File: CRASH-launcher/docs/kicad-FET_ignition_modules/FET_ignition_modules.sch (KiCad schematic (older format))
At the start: 22 parts, among them P1 CONN_1, P1 CONN_6, P2 CONN_1, P2 CONN_2, P3 CONN_1, Q1 FET_N, Q2 FET_N, U1 TSC888, U2 TSC888

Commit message: second shot at module PCB
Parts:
- removed P1, P2: CONN_1, symbol CONN_1
- added P4: CONN_1, symbol CONN_1
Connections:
- net GNDPWR: now also P4.1
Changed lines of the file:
@@
-EESchema Schematic File Version 2  date Fri 15 Jun 2012 12:45:23 AM MDT
+EESchema Schematic File Version 2  date Fri 15 Jun 2012 01:25:22 AM MDT
 LIBS:bryan_custom
 LIBS:power
@@
 Comment4 ""
 $EndDescr
-Connection ~ 9450 6550
-Connection ~ 9450 6400
 $Comp
-L CONN_1 P2
-U 1 1 4FDAD9F2
-P 9600 6550
-F 0 "P2" H 9680 6550 40  0000 L CNN
-F 1 "CONN_1" H 9600 6605 30  0001 C CNN
-	1    9600 6550
-	1    0    0    -1
-$EndComp
-$Comp
-L CONN_1 P1
-U 1 1 4FDAD9EC
+L CONN_1 P4
+U 1 1 4FDADA40
 P 9600 6400
-F 0 "P1" H 9680 6400 40  0000 L CNN
+F 0 "P4" H 9680 6400 40  0000 L CNN
 F 1 "CONN_1" H 9600 6455 30  0001 C CNN
 	1    9600 6400
 	1    0    0    -1
 $EndComp
-Connection ~ 7100 3500
 $Comp
 L CONN_1 P3
-U 1 1 4FDAD9BF
+U 1 1 4FDADA3B
 P 7250 3500
 F 0 "P3" H 7330 3500 40  0000 L CNN
@@
 	1    0    0    -1
 $EndComp
+Connection ~ 9450 6400
+Connection ~ 7100 3500
 Connection ~ 5500 3900
 Wire Wire Line

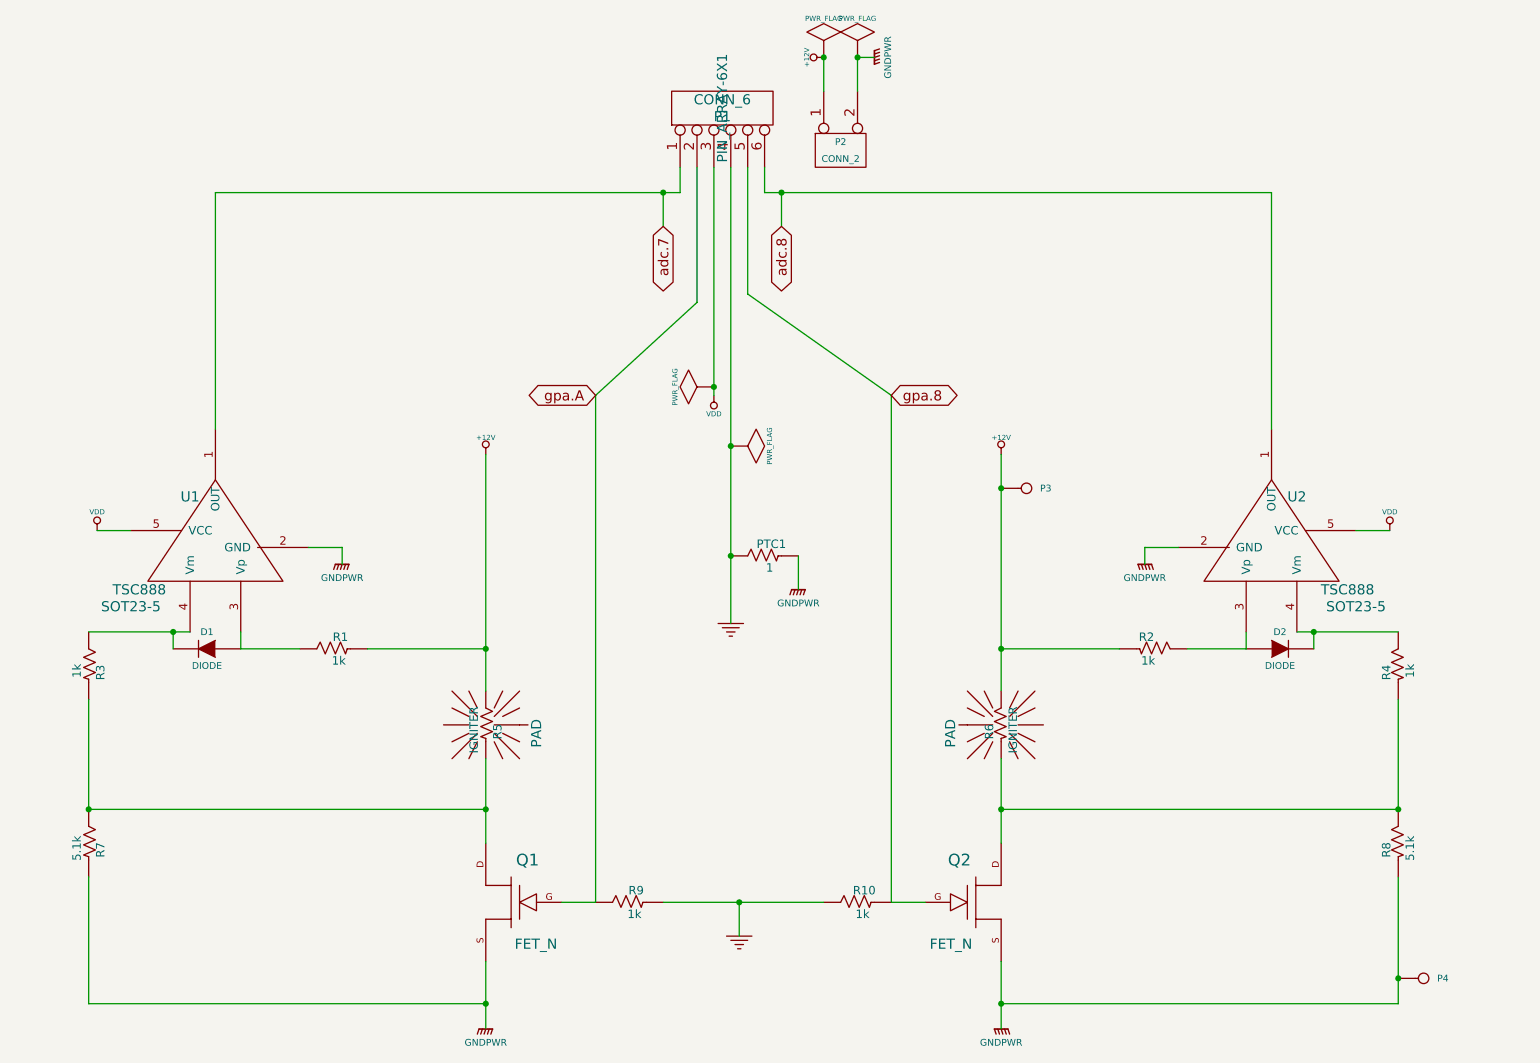
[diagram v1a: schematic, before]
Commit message: rounded corners on PCB zones, removed VDD rectangle, other suggestions from sgrace
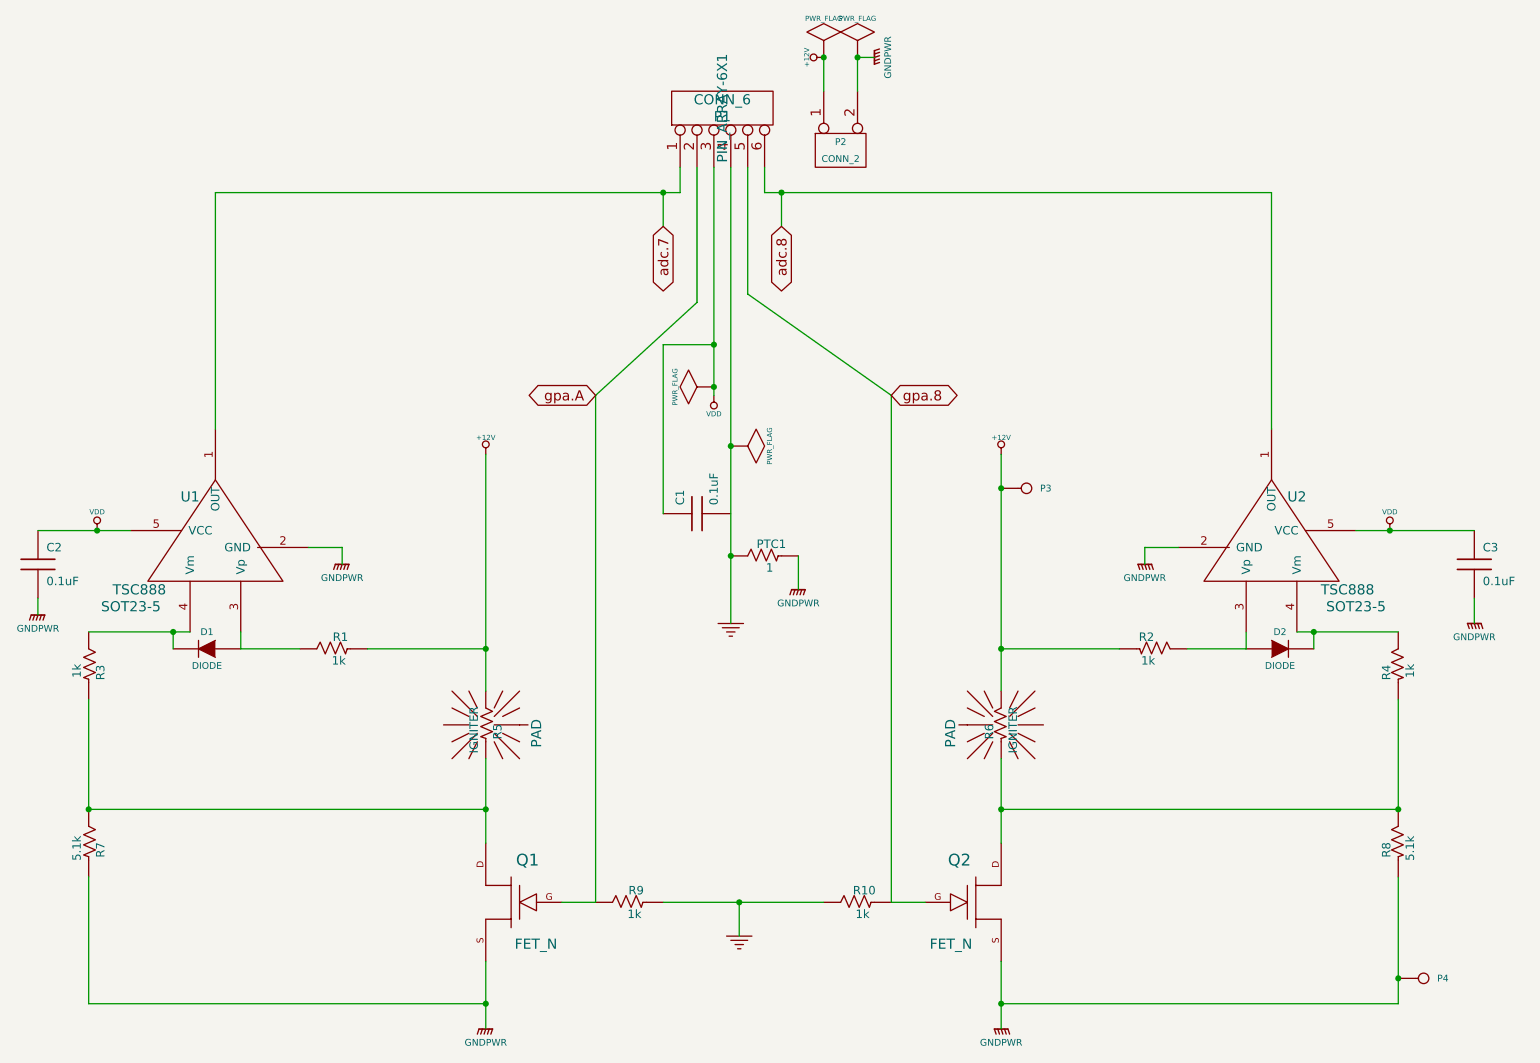
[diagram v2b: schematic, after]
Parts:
- added C1, C2, C3: 0.1uF, symbol C
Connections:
- net GNDPWR: now also C2.2, C3.2
- net VDD: now also C1.1, C2.1, C3.1

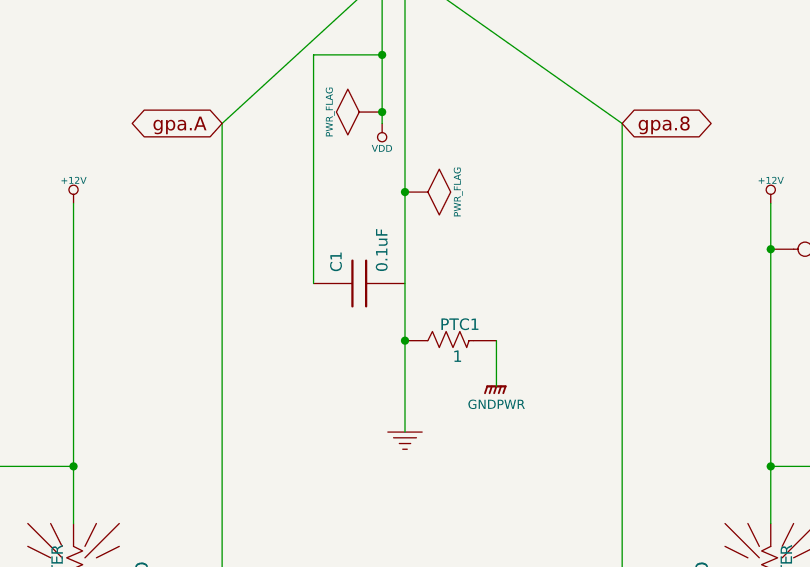
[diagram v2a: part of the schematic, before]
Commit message: rounded corners, plopped in a few missing caps on gpios and adc
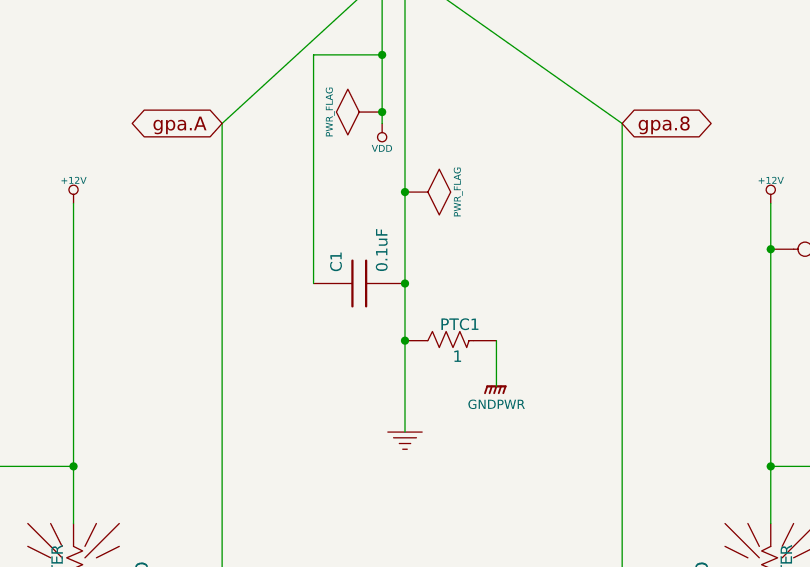
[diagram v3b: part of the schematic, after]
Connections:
- net GND: now also C1.2
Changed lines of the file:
@@
-EESchema Schematic File Version 2  date Fri 15 Jun 2012 06:22:16 PM MDT
+EESchema Schematic File Version 2  date Tue 03 Jul 2012 10:38:54 AM MDT
 LIBS:bryan_custom
 LIBS:power
@@
 Sheet 1 1
 Title ""
-Date "16 jun 2012"
+Date "17 jun 2012"
 Rev ""
 Comp ""
@@
 Comment4 ""
 $EndDescr
+Connection ~ 5500 3650
 Connection ~ 5400 2650
 Wire Wire Line
@@
 $EndComp
 $Comp
-L GNDPWR #PWR13
+L GNDPWR #PWR01
 U 1 1 4FDBCF69
 P 9900 4300
-F 0 "#PWR13" H 9900 4350 40  0001 C CNN
+F 0 "#PWR01" H 9900 4350 40  0001 C CNN
 F 1 "GNDPWR" H 9900 4220 40  0000 C CNN
 	1    9900 4300
@@
 $EndComp
 $Comp
-L GNDPWR #PWR11
+L GNDPWR #PWR02
 U 1 1 4FDBCF4D
 P 1400 4250
-F 0 "#PWR11" H 1400 4300 40  0001 C CNN
+F 0 "#PWR02" H 1400 4300 40  0001 C CNN
 F 1 "GNDPWR" H 1400 4170 40  0000 C CNN
 	1    1400 4250
@@
 $EndComp
 $Comp
-L GNDPWR #PWR10
+L GNDPWR #PWR03
 U 1 1 4FD97A60
 P 5900 4100
-F 0 "#PWR10" H 5900 4150 40  0001 C CNN
+F 0 "#PWR03" H 5900 4150 40  0001 C CNN
 F 1 "GNDPWR" H 5900 4020 40  0000 C CNN
 	1    5900 4100
@@
 $EndComp
 $Comp
-L PWR_FLAG #FLG3
+L PWR_FLAG #FLG04
 U 1 1 4FD97533
 P 5400 2900
-F 0 "#FLG3" H 5400 3170 30  0001 C CNN
+F 0 "#FLG04" H 5400 3170 30  0001 C CNN
 F 1 "PWR_FLAG" H 5400 3130 30  0000 C CNN
 	1    5400 2900
@@
 $EndComp
 $Comp
-L GND #PWR14
+L GND #PWR05
 U 1 1 4FD9750F
 P 5550 6150
-F 0 "#PWR14" H 5550 6150 30  0001 C CNN
+F 0 "#PWR05" H 5550 6150 30  0001 C CNN
 F 1 "GND" H 5550 6080 30  0001 C CNN
 	1    5550 6150
@@
 $EndComp
 $Comp
-L PWR_FLAG #FLG4
+L PWR_FLAG #FLG06
 U 1 1 4FD974CA
 P 5500 3250
-F 0 "#FLG4" H 5500 3520 30  0001 C CNN
+F 0 "#FLG06" H 5500 3520 30  0001 C CNN
 F 1 "PWR_FLAG" H 5500 3480 30  0000 C CNN
 	1    5500 3250
@@
 $EndComp
 $Comp
-L PWR_FLAG #FLG1
+L PWR_FLAG #FLG07
 U 1 1 4FD974B2
 P 6050 950
-F 0 "#FLG1" H 6050 1220 30  0001 C CNN
+F 0 "#FLG07" H 6050 1220 30  0001 C CNN
 F 1 "PWR_FLAG" H 6050 1180 30  0000 C CNN
 	1    6050 950
@@
 $EndComp
 $Comp
-L PWR_FLAG #FLG2
+L PWR_FLAG #FLG08
 U 1 1 4FD974AA
 P 6250 950
-F 0 "#FLG2" H 6250 1220 30  0001 C CNN
+F 0 "#FLG08" H 6250 1220 30  0001 C CNN
 F 1 "PWR_FLAG" H 6250 1180 30  0000 C CNN
 	1    6250 950
@@
 $EndComp
 $Comp
-L +12V #PWR5
+L +12V #PWR09
 U 1 1 4FD97473
 P 7100 3300
-F 0 "#PWR5" H 7100 3250 20  0001 C CNN
+F 0 "#PWR09" H 7100 3250 20  0001 C CNN
 F 1 "+12V" H 7100 3400 30  0000 C CNN
 	1    7100 3300
@@
 $EndComp
 $Comp
-L VDD #PWR7
+L VDD #PWR010
 U 1 1 4FD973FA
 P 9400 3750
-F 0 "#PWR7" H 9400 3850 30  0001 C CNN
+F 0 "#PWR010" H 9400 3850 30  0001 C CNN
 F 1 "VDD" H 9400 3860 30  0000 C CNN
 	1    9400 3750
@@
 $EndComp
 $Comp
-L GNDPWR #PWR9
+L GNDPWR #PWR011
 U 1 1 4FD973F6
 P 7950 3950
-F 0 "#PWR9" H 7950 4000 40  0001 C CNN
+F 0 "#PWR011" H 7950 4000 40  0001 C CNN
 F 1 "GNDPWR" H 7950 3870 40  0000 C CNN
 	1    7950 3950
@@
 $EndComp
 $Comp
-L GNDPWR #PWR16
+L GNDPWR #PWR012
 U 1 1 4FD973F5
 P 7100 6700
-F 0 "#PWR16" H 7100 6750 40  0001 C CNN
+F 0 "#PWR012" H 7100 6750 40  0001 C CNN
 F 1 "GNDPWR" H 7100 6620 40  0000 C CNN
 	1    7100 6700
@@
 $EndComp
 $Comp
-L VDD #PWR3
+L VDD #PWR013
 U 1 1 4FD9738F
 P 5400 2950
-F 0 "#PWR3" H 5400 3050 30  0001 C CNN
+F 0 "#PWR013" H 5400 3050 30  0001 C CNN
 F 1 "VDD" H 5400 3060 30  0000 C CNN
 	1    5400 2950
@@
 $EndComp
 $Comp
-L GNDPWR #PWR15
+L GNDPWR #PWR014
 U 1 1 4FD97309
 P 4050 6700
-F 0 "#PWR15" H 4050 6750 40  0001 C CNN
+F 0 "#PWR014" H 4050 6750 40  0001 C CNN
 F 1 "GNDPWR" H 4050 6620 40  0000 C CNN
 	1    4050 6700
@@
 $EndComp
 $Comp
-L GNDPWR #PWR8
+L GNDPWR #PWR015
 U 1 1 4FD972F7
 P 3200 3950
-F 0 "#PWR8" H 3200 4000 40  0001 C CNN
+F 0 "#PWR015" H 3200 4000 40  0001 C CNN
 F 1 "GNDPWR" H 3200 3870 40  0000 C CNN
 	1    3200 3950
@@
 $EndComp
 $Comp
-L GND #PWR12
+L GND #PWR016
 U 1 1 4FD972A1
 P 5500 4300
-F 0 "#PWR12" H 5500 4300 30  0001 C CNN
+F 0 "#PWR016" H 5500 4300 30  0001 C CNN
 F 1 "GND" H 5500 4230 30  0001 C CNN
 	1    5500 4300
@@
 $EndComp
 $Comp
-L +12V #PWR1
+L +12V #PWR017
 U 1 1 4FD9729F
 P 6050 950
-F 0 "#PWR1" H 6050 900 20  0001 C CNN
+F 0 "#PWR017" H 6050 900 20  0001 C CNN
 F 1 "+12V" H 6050 1050 30  0000 C CNN
 	1    6050 950
@@
 $EndComp
 $Comp
-L GNDPWR #PWR2
+L GNDPWR #PWR018
 U 1 1 4FD9729E
 P 6350 950
-F 0 "#PWR2" H 6350 1000 40  0001 C CNN
+F 0 "#PWR018" H 6350 1000 40  0001 C CNN
 F 1 "GNDPWR" H 6350 870 40  0000 C CNN
 	1    6350 950
@@
 $EndComp
 $Comp
-L VDD #PWR6
+L VDD #PWR019
 U 1 1 4FD96DF9
 P 1750 3750
-F 0 "#PWR6" H 1750 3850 30  0001 C CNN
+F 0 "#PWR019" H 1750 3850 30  0001 C CNN
 F 1 "VDD" H 1750 3860 30  0000 C CNN
 	1    1750 3750
@@
 $EndComp
 $Comp
-L +12V #PWR4
+L +12V #PWR020
 U 1 1 4F2C9CBE
 P 4050 3300
-F 0 "#PWR4" H 4050 3250 20  0001 C CNN
+F 0 "#PWR020" H 4050 3250 20  0001 C CNN
 F 1 "+12V" H 4050 3400 30  0000 C CNN
 	1    4050 3300
